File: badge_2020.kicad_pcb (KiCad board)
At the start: 2 copper layers, 22 parts, among them J1 USB_A, Q1 AOI409 (LP0701N3-G), SW1 SW_Push, SW2 SW, U1 ATTINY85-20PU

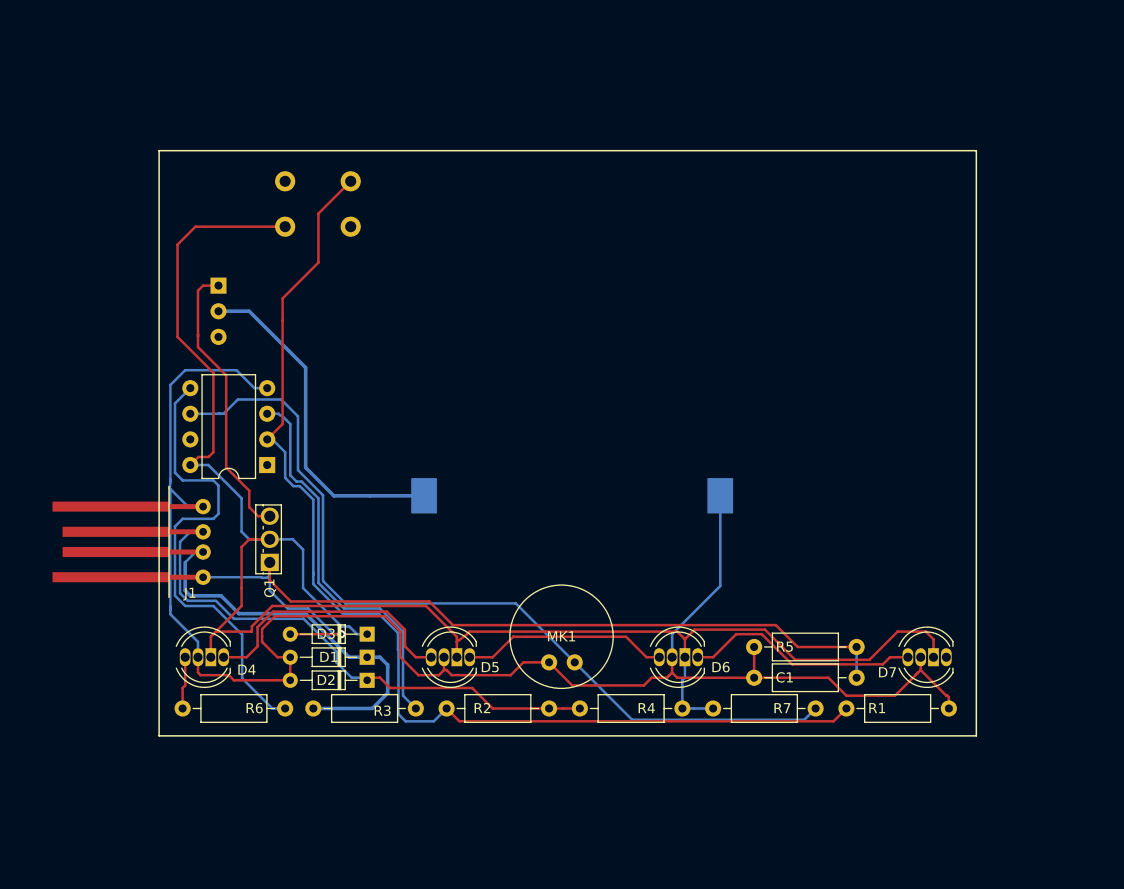
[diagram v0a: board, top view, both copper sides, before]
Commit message: revisado y actualizado
Esta versión debería funcionar. Falta el silkscreen posterior, y quizá cambiar la huella del interruptor
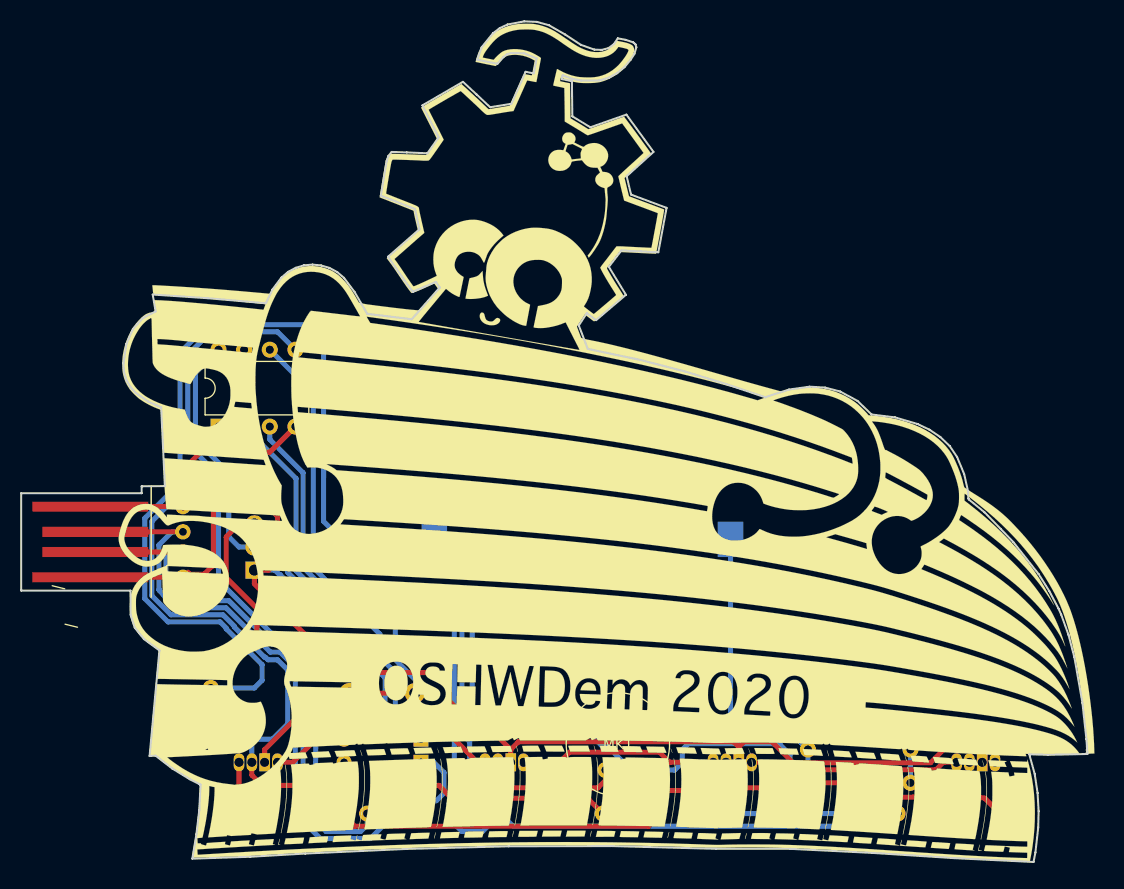
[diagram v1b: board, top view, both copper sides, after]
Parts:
- added ?: , , F.Cu at (120.4, 117.3)
- added ?: , , F.Cu at (121.7, 121.2)
- added G***: LOGO, Project_Footprint_Library:•OSHWI_footprint_silk, F.Cu at (175.5, 107.7)
- added G***: LOGO, Project_Footprint_Library:mask, B.Cu at (330.2, 211.8)
- added G***: LOGO, Project_Footprint_Library:mask, F.Cu at (330.2, 211.3)
- C1, D1, D2, D3, D4, D5, D6, D7, R1, R2, R3, R4, R5, R6, R7: moved to B.Cu
- MK1: value LD-MC-0905P -> 0905P
- Q1: value AOI409 (LP0701N3-G) -> AOI409; moved to B.Cu
- moved SW1 46.7 mm to (148.8, 127.8)
- moved SW2 37.3 mm to (135.1, 124.7)
- moved MK1 12.0 mm to (173.0, 132.8)
- moved D4 11.7 mm to (141.7, 134.6)
- moved D5 11.7 mm to (166.1, 134.6)
- moved D6 11.7 mm to (188.7, 134.6)
- moved C1 11.7 mm to (204.5, 136.7)
- moved D1 11.7 mm to (156.0, 134.6)
- moved D2 11.7 mm to (156.0, 136.9)
- moved D3 11.7 mm to (156.0, 132.3)
- moved R2 11.7 mm to (174.0, 139.7)
- moved R3 11.7 mm to (150.6, 139.7)
- moved R4 11.7 mm to (177.0, 139.7)
- moved R6 11.7 mm to (147.8, 139.7)
- moved R7 11.7 mm to (200.4, 139.7)
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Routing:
- net Net-(BT1-Pad1): track 33.7 -> 93.8 mm
- net Net-(C1-Pad1): track 89.2 -> 131.8 mm, vias 1 -> 0
- net GND: track 166.0 -> 198.4 mm
- net Net-(D1-Pad1): track 38.9 -> 69.9 mm
- net Net-(R6-Pad1): track 46.4 -> 76.2 mm
- net Net-(D2-Pad1): track 53.7 -> 78.0 mm, vias 0 -> 1
- net Net-(D3-Pad1): track 171.8 -> 153.4 mm
- net Net-(MK1-Pad2): track 84.5 -> 101.2 mm
- net Net-(R3-Pad2): track 38.4 -> 53.4 mm
- net Net-(Q1-Pad3): track 28.5 -> 20.1 mm
- net Net-(D4-Pad1): track 26.4 -> 23.7 mm
- net Net-(D6-Pad1): track 23.3 -> 20.9 mm
- net Net-(R1-Pad2): track 110.9 -> 111.7 mm
- net Net-(D5-Pad1): track 20.5 -> 19.6 mm
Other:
- board outline added: 105.7 x 83.3 mm
- net class Default: trace_width 0.25 -> 0.5
- net class power: trace_width 0.35 -> 0.5
- rule trace_min: 0.2 -> 0.5

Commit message: Retoques menores
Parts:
- removed the G*** at (330.2, 211.3)
- moved G*** 0.36 mm to (175.8, 107.4)

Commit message: Actualizado con trasera
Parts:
- removed ? (x2): , 
- removed the G*** at (175.8, 107.4)
- removed the G*** at (330.2, 211.8)
- added G***: LOGO, Project_Footprint_Library:BricoLabs_logo_2cm, B.Cu at (199.9, 114.0)
- added G***: LOGO, Project_Footprint_Library:amtega_logo_2cm, B.Cu at (151.4, 122.7)
- added G***: LOGO, Project_Footprint_Library:•OSHWI_footprint_silk_F, F.Cu at (174.8, 103.1)
- moved SW1 49.1 mm to (197.9, 130.3)
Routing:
- net Net-(D3-Pad1): track 153.4 -> 186.2 mm
- net Net-(R1-Pad2): track 111.7 -> 124.3 mm
- net Net-(D4-Pad1): track 23.7 -> 27.9 mm
- net GND: track 198.4 -> 201.1 mm

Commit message: Actualización
Versión corregida y actualizada
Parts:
- removed the D1 at (156.0, 134.6)
- removed G***: LOGO, Project_Footprint_Library:BricoLabs_logo_2cm
- removed G***: LOGO, Project_Footprint_Library:amtega_logo_2cm
- removed G***: LOGO, Project_Footprint_Library:•OSHWI_footprint_silk_F
- removed the R5 at (194.3, 133.3)
- added C2: 10uF, Capacitor_THT:CP_Radial_D5.0mm_P2.50mm, B.Cu at (166.4, 135.1)
- added D3: BZX55 3V6, Diode_THT:D_DO-34_SOD68_P7.62mm_Horizontal, B.Cu at (156.0, 136.9)
- added D8: WS2812D, LED_THT:LED_D5.0mm-WS2812D, B.Cu at (138.7, 126.0)
- added Imagen_1: IMAGEN OSHWI, project footprints:•OSHWI_footprint_silk, F.Cu at (175.8, 107.4)
- added Imagen_2: LOGO AMTEGA, project footprints:amtega_logo_2cm, B.Cu at (194.6, 125.2)
- added Imagen_3: LOGO BRICOLABS, project footprints:BricoLabs_logo_small, B.Cu at (212.9, 122.7)
- added R1: 100K, Resistor_THT:R_Axial_DIN0207_L6.3mm_D2.5mm_P10.16mm_Horizontal, B.Cu at (190.2, 136.7)
- C1: footprint Resistor_THT:R_Axial_DIN0207_L6.3mm_D2.5mm_P10.16mm_Horizontal -> Capacitor_THT:C_Disc_D4.3mm_W1.9mm_P5.00mm
- D2: value BAT41 -> BZX55 3V6
- R6: renamed from R7; value 2K2 -> 10K
- moved D7 74.1 mm to (143.5, 108.5), turned to 0 degrees
- moved D6 66.6 mm to (133.1, 98.0), turned to 0 degrees
- moved D4 63.8 mm to (201.7, 112.8), turned to 0 degrees
- moved D5 31.9 mm to (185.7, 109.5), turned to 0 degrees
- moved C1 22.4 mm to (182.1, 136.9), turned to 0 degrees
- moved R7 14.3 mm to (200.4, 133.6)
- moved U1 12.7 mm to (148.6, 102.4)
- moved SW1 12.5 mm to (205.2, 140.5)
- moved R5 10.2 mm to (137.7, 139.7), turned to 0 degrees
- moved BT1 4.58 mm to (172.2, 117.1)
- moved D2 2.29 mm to (156.0, 134.6)
- renumbered D3 to D1, R4 to R2, R2 to R3, R3 to R4, R6 to R5, R1 to R7
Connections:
- net Net-(Q1-Pad3) renamed /D
- D7 pad 1: (no net) -> Net-(D7-Pad1)
- J1 pad 2: Net-(D1-Pad1) -> Net-(D2-Pad1)
- J1 pad 3: Net-(D2-Pad1) -> Net-(D3-Pad1)
- R3 pad 1: Net-(D2-Pad1) -> Net-(D3-Pad1)
- R3 pad 2: Net-(R1-Pad2) -> Net-(R3-Pad2)
- R4 pad 1: Net-(D1-Pad1) -> Net-(D2-Pad1)
- R4 pad 2: Net-(R3-Pad2) -> Net-(R4-Pad2)
- R7 pad 2: Net-(R1-Pad2) -> Net-(R7-Pad2)
- SW1 pad 2: Net-(R1-Pad2) -> Net-(R7-Pad2)
- U1 pad 2: Net-(R1-Pad2) -> Net-(R4-Pad2)
- U1 pad 6: Net-(MK1-Pad2) -> Net-(R7-Pad2)
- U1 pad 7: (no net) -> Net-(MK1-Pad2)
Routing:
- net Net-(R1-Pad2): track 124.3 -> 0.00 mm
- net Net-(R7-Pad2): track 0.00 -> 101.8 mm
- net Net-(D4-Pad4): track 5.19 -> 100.1 mm
- net Net-(D3-Pad1): track 0.00 -> 75.4 mm
- net GND: track 201.1 -> 275.4 mm
- net Net-(D1-Pad1): track 69.9 -> 0.00 mm
- net Net-(C2-Pad1): track 186.2 -> 231.5 mm
- net Net-(R4-Pad2): track 0.00 -> 41.8 mm
- net Net-(D5-Pad1): track 19.6 -> 53.5 mm
- net Net-(C1-Pad1): track 132.0 -> 105.0 mm
- net Net-(D7-Pad1): track 0.00 -> 17.9 mm
- net Net-(D4-Pad1): track 27.9 -> 13.6 mm
- net Net-(R3-Pad2): track 53.4 -> 43.4 mm
- net Net-(MK1-Pad2): track 101.2 -> 94.1 mm
- net Net-(R5-Pad1): track 76.2 -> 72.4 mm
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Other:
- outline, holes or cut-outs redrawn
- board text added: "+"
- board text added: "GND"
